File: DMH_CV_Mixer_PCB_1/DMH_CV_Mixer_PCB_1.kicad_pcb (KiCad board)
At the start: 2 copper layers, 48 x 175 mm, 23 parts, among them J0 Conn_01x01, J1 TS_Jack_6.35mm_Sw, J10 TS_Jack_6.35mm_Sw, J100 IDC_02x05, J11 TS_Jack_6.35mm_Sw, J12 TS_Jack_6.35mm_Sw, J13 Conn_01x16, J2 TS_Jack_6.35mm_Sw, J3 TS_Jack_6.35mm_Sw, J4 TS_Jack_6.35mm_Sw, J5 TS_Jack_6.35mm_Sw, J50 Conn_01x06, J6 TS_Jack_6.35mm_Sw, J60 Conn_01x06, J7 TS_Jack_6.35mm_Sw, J8 TS_Jack_6.35mm_Sw, J9 TS_Jack_6.35mm_Sw

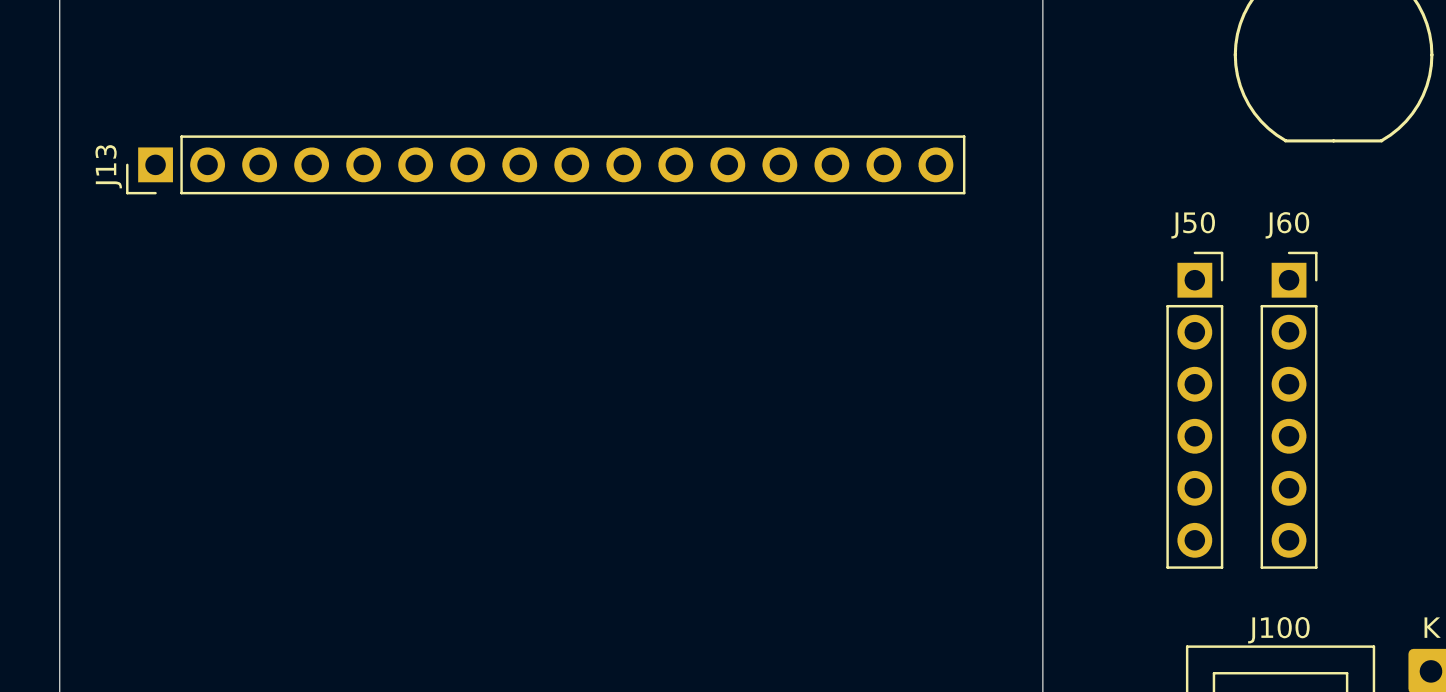
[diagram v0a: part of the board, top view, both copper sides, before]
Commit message: Finished IO page
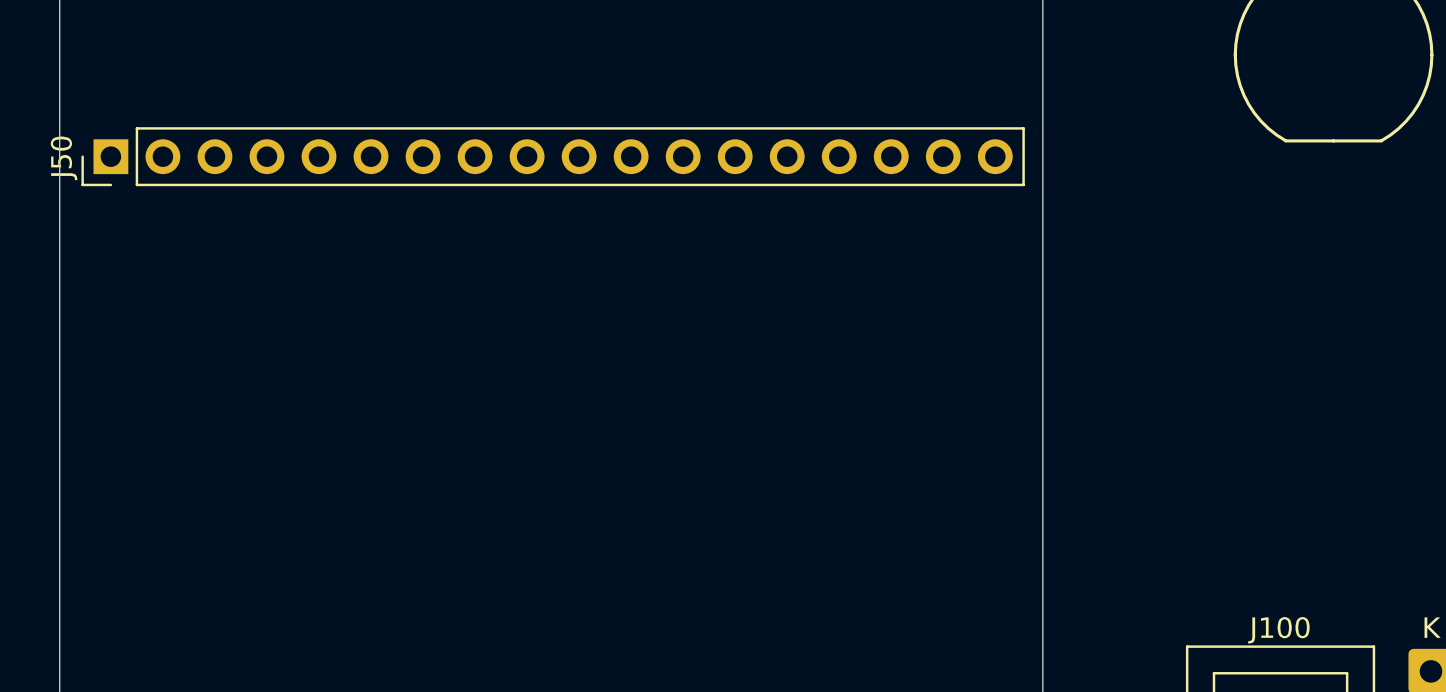
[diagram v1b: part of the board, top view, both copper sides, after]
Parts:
- removed J13: Conn_01x16, Connector_PinHeader_2.54mm:PinHeader_1x16_P2.54mm_Vertical
- removed J60: Conn_01x06, Connector_PinSocket_2.54mm:PinSocket_1x06_P2.54mm_Vertical
- J50: value Conn_01x06 -> Conn_01x18; footprint Connector_PinSocket_2.54mm:PinSocket_1x06_P2.54mm_Vertical -> Connector_PinHeader_2.54mm:PinHeader_1x18_P2.54mm_Vertical
- moved J50 53.3 mm to (53.5, 176.8), turned to 90 degrees
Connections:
- J1 pad S: unconnected-(J1-PadS) -> GND
- J1 pad T: unconnected-(J1-PadT) -> Net-(J50-Pin_2)
- J10 pad S: unconnected-(J10-PadS) -> GND
- J10 pad T: unconnected-(J10-PadT) -> Net-(J50-Pin_14)
- J11 pad S: unconnected-(J11-PadS) -> GND
- J11 pad T: unconnected-(J11-PadT) -> Net-(J50-Pin_15)
- J12 pad S: unconnected-(J12-PadS) -> GND
- J12 pad T: unconnected-(J12-PadT) -> Net-(J50-Pin_16)
- J12 pad TN: unconnected-(J12-PadTN) -> Net-(J50-Pin_17)
- J2 pad S: unconnected-(J2-PadS) -> GND
- J2 pad T: unconnected-(J2-PadT) -> Net-(J50-Pin_3)
- J3 pad S: unconnected-(J3-PadS) -> GND
- J3 pad T: unconnected-(J3-PadT) -> Net-(J50-Pin_4)
- J3 pad TN: unconnected-(J3-PadTN) -> Net-(J50-Pin_5)
- J4 pad S: unconnected-(J4-PadS) -> GND
- J4 pad T: unconnected-(J4-PadT) -> Net-(J50-Pin_6)
- J5 pad S: unconnected-(J5-PadS) -> GND
- J5 pad T: unconnected-(J5-PadT) -> Net-(J50-Pin_7)
- J50 pad 1: unconnected-(J50-Pin_1-Pad1) -> GND
- J50 pad 2: unconnected-(J50-Pin_2-Pad2) -> Net-(J50-Pin_2)
- J50 pad 3: unconnected-(J50-Pin_3-Pad3) -> Net-(J50-Pin_3)
- J50 pad 4: unconnected-(J50-Pin_4-Pad4) -> Net-(J50-Pin_4)
- J50 pad 5: unconnected-(J50-Pin_5-Pad5) -> Net-(J50-Pin_5)
- J50 pad 6: unconnected-(J50-Pin_6-Pad6) -> Net-(J50-Pin_6)
- J6 pad S: unconnected-(J6-PadS) -> GND
- J6 pad T: unconnected-(J6-PadT) -> Net-(J50-Pin_8)
- J6 pad TN: unconnected-(J6-PadTN) -> Net-(J50-Pin_9)
- J7 pad S: unconnected-(J7-PadS) -> GND
- J7 pad T: unconnected-(J7-PadT) -> Net-(J50-Pin_10)
- J8 pad S: unconnected-(J8-PadS) -> GND
- J8 pad T: unconnected-(J8-PadT) -> Net-(J50-Pin_11)
- J9 pad S: unconnected-(J9-PadS) -> GND
- J9 pad T: unconnected-(J9-PadT) -> Net-(J50-Pin_12)
- J9 pad TN: unconnected-(J9-PadTN) -> Net-(J50-Pin_13)
